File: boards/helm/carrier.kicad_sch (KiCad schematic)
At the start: 22 parts, among them J1 OPI_Z3_26PIN, J10 AUX 5V (screen), J16 BATT 12V, J2 OPI_BREAKOUT, J3 UART5 ttyAS5, J4 UART2 ttyAS2, J8 I2C3 spare, J9 FAN 5V, Q1 IRF9540N, U5 XL4015 5A

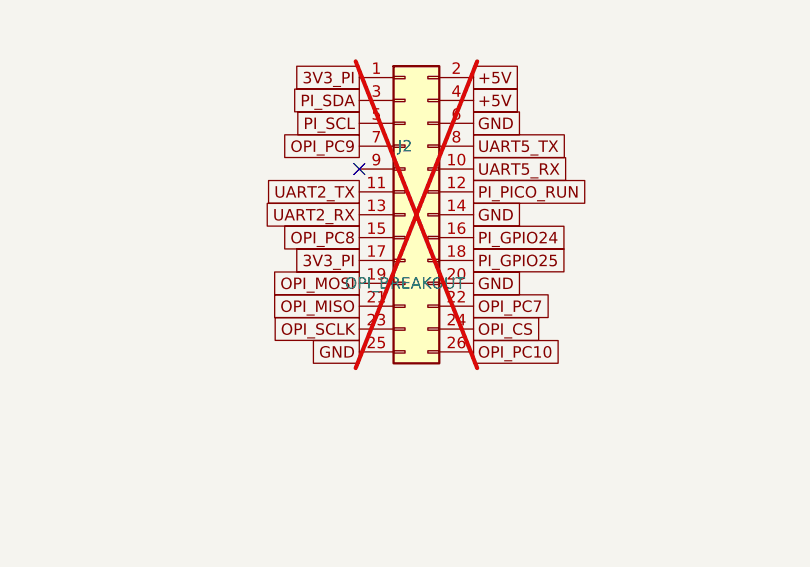
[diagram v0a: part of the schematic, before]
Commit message: feat(helm): J2 doubles as Raspberry Pi port (classic 26-pin positions), silk + docs
The PI26 net map already follows the classic RPi 26-pin layout, so a
Raspberry Pi (40-pin header pins 1-26) drops onto J2 via the same 26-way
IDC ribbon: power, Pico I2C link (SDA1/SCL1), console UART (TXD0/RXD0),
SPI and SWD/RUN GPIOs all line up. Fit one SBC only; J4 'UART2' JST is
bit-bang-only on an RPi (pins 11/13 are plain GPIOs there).

Co-Authored-By: Claude Fable 5 <noreply@anthropic.com>
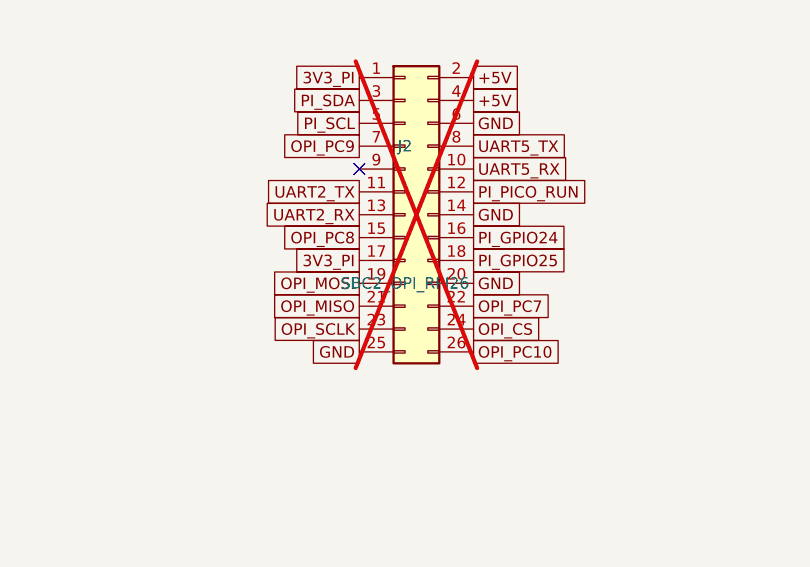
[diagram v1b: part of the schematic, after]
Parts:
- J2: value OPI_BREAKOUT -> SBC2_OPI_RPI26
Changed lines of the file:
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@@
     (property "Reference" "J2" (at 149.86 196.85 0)
       (effects (font (size 1.27 1.27))))
-    (property "Value" "OPI_BREAKOUT" (at 149.86 212.09 0)
+    (property "Value" "SBC2_OPI_RPI26" (at 149.86 212.09 0)
       (effects (font (size 1.27 1.27))))
     (property "Footprint" "Connector_PinHeader_2.54mm:PinHeader_2x13_P2.54mm_Vertical" (at 149.86 204.47 0)

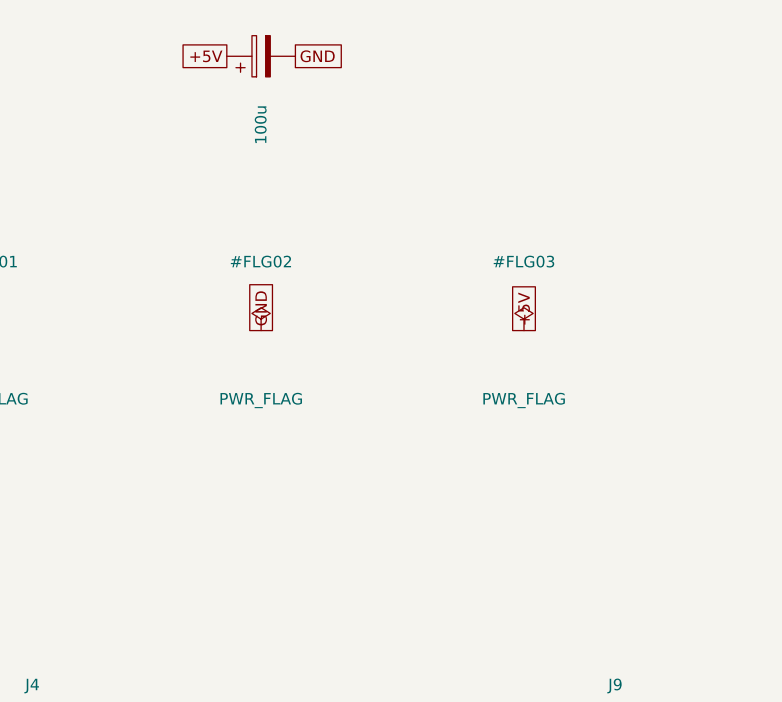
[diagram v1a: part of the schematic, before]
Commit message: feat(helm): NMEA2000/CAN provision — J5 power/shield connector, VIN tap, CAN-on-J12 docs
CAN rides the Pico 2 (can2040 on GP18/GP19); a 3.3V transceiver module
(Waveshare SN65HVD230) plugs J12 pins 1/8/6/7. New J5 XH-3 lands the N2K
drop cable's V+/GND/SHIELD; R41 (0R DNP) optionally powers the backbone
from VIN, R42 (0R DNP) bonds shield to GND. DRC 0/0.

Co-Authored-By: Claude Fable 5 <noreply@anthropic.com>
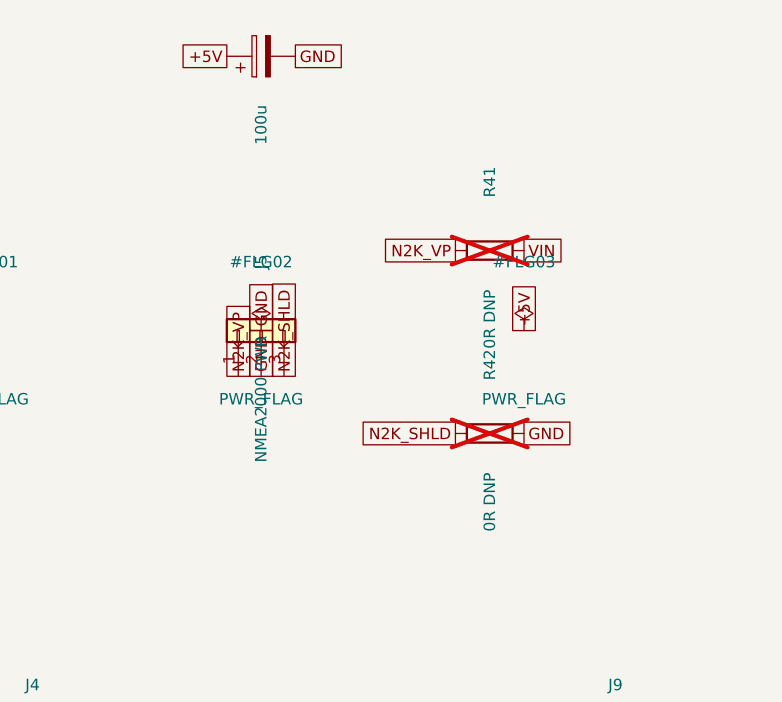
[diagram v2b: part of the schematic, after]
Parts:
- added J5: NMEA2000 PWR, Connector_JST:JST_XH_B3B-XH-A_1x03_P2.50mm_Vertical, symbol Connector_Generic:Conn_01x03
- added R41, R42: 0R DNP, Resistor_SMD:R_0805_2012Metric, symbol Device:R
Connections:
- net GND: now also J5.2 (Pin_2), R42.2
- net VIN: now also R41.2
- new net N2K_SHLD: J5.3 (Pin_3), R42.1
- new net N2K_VP: J5.1 (Pin_1), R41.1
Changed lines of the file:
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@@
     (effects (font (size 2 2) (bold yes)) (justify left bottom))
+  )
+  (symbol (lib_id "Connector_Generic:Conn_01x03") (at 330.2 138.43 90) (unit 1)
+    (exclude_from_sim no) (in_bom yes) (on_board yes) (dnp no)
+    (property "Reference" "J5" (at 330.2 130.81 0)
+      (effects (font (size 1.27 1.27))))
+    (property "Value" "NMEA2000 PWR" (at 330.2 146.05 0)
+      (effects (font (size 1.27 1.27))))
+    (property "Footprint" "Connector_JST:JST_XH_B3B-XH-A_1x03_P2.50mm_Vertical" (at 330.2 138.43 0)
+      (effects (font (size 1.27 1.27)) (hide yes)))
+    (property "Datasheet" "" (at 330.2 138.43 0)
+      (effects (font (size 1.27 1.27)) (hide yes)))
+    (property "MPN" "JST B4B-XH-A(LF)(SN)" (at 330.2 138.43 0)
+      (effects (font (size 1.27 1.27)) (hide yes)))
+    (pin "1")
+    (pin "2")
+    (pin "3")
+    (instances (project "vanchor-helm" (path "/a0000000-0000-4000-8000-000000000001/c0000000-0000-4000-8000-000000000002" (reference "J5") (unit 1))))
+  )
+  (symbol (lib_id "Device:R") (at 355.6 129.54 90) (unit 1)
+    (exclude_from_sim no) (in_bom yes) (on_board yes) (dnp yes)
+    (property "Reference" "R41" (at 355.6 121.92 0)
+      (effects (font (size 1.27 1.27))))
+    (property "Value" "0R DNP" (at 355.6 137.16 0)
+      (effects (font (size 1.27 1.27))))
+    (property "Footprint" "Resistor_SMD:R_0805_2012Metric" (at 355.6 129.54 0)
+      (effects (font (size 1.27 1.27)) (hide yes)))
+    (property "Datasheet" "" (at 355.6 129.54 0)
+      (effects (font (size 1.27 1.27)) (hide yes)))
+    (pin "1")
+    (pin "2")
+    (instances (project "vanchor-helm" (path "/a0000000-0000-4000-8000-000000000001/c0000000-0000-4000-8000-000000000002" (reference "R41") (unit 1))))
+  )
+  (symbol (lib_id "Device:R") (at 355.6 149.86 90) (unit 1)
+    (exclude_from_sim no) (in_bom yes) (on_board yes) (dnp yes)
+    (property "Reference" "R42" (at 355.6 142.24 0)
+      (effects (font (size 1.27 1.27))))
+    (property "Value" "0R DNP" (at 355.6 157.48 0)
+      (effects (font (size 1.27 1.27))))
+    (property "Footprint" "Resistor_SMD:R_0805_2012Metric" (at 355.6 149.86 0)
+      (effects (font (size 1.27 1.27)) (hide yes)))
+    (property "Datasheet" "" (at 355.6 149.86 0)
+      (effects (font (size 1.27 1.27)) (hide yes)))
+    (pin "1")
+    (pin "2")
+    (instances (project "vanchor-helm" (path "/a0000000-0000-4000-8000-000000000001/c0000000-0000-4000-8000-000000000002" (reference "R42") (unit 1))))
   )
   (symbol (lib_id "Connector_Generic:Conn_01x02") (at 44.45 69.85 0) (unit 1)
@@
     (instances (project "vanchor-helm" (path "/a0000000-0000-4000-8000-000000000001/c0000000-0000-4000-8000-000000000002" (reference "#FLG04") (unit 1))))
   )
+  (global_label "N2K_VP" (shape passive) (at 327.66 143.51 270.0) (fields_autoplaced yes)
+    (effects (font (size 1.27 1.27)) (justify left))
+    (property "Intersheetrefs" "${INTERSHEET_REFS}" (at 327.66 143.51 0)
+      (effects (font (size 1.27 1.27)) (hide yes)))
+  )
+  (global_label "GND" (shape passive) (at 330.2 143.51 270.0) (fields_autoplaced yes)
+    (effects (font (size 1.27 1.27)) (justify left))
+    (property "Intersheetrefs" "${INTERSHEET_REFS}" (at 330.2 143.51 0)
+      (effects (font (size 1.27 1.27)) (hide yes)))
+  )
+  (global_label "N2K_SHLD" (shape passive) (at 332.74 143.51 270.0) (fields_autoplaced yes)
+    (effects (font (size 1.27 1.27)) (justify left))
+    (property "Intersheetrefs" "${INTERSHEET_REFS}" (at 332.74 143.51 0)
+      (effects (font (size 1.27 1.27)) (hide yes)))
+  )
+  (global_label "N2K_VP" (shape passive) (at 351.79 129.54 180.0) (fields_autoplaced yes)
+    (effects (font (size 1.27 1.27)) (justify right))
+    (property "Intersheetrefs" "${INTERSHEET_REFS}" (at 351.79 129.54 0)
+      (effects (font (size 1.27 1.27)) (hide yes)))
+  )
+  (global_label "VIN" (shape passive) (at 359.41 129.54 0.0) (fields_autoplaced yes)
+    (effects (font (size 1.27 1.27)) (justify left))
+    (property "Intersheetrefs" "${INTERSHEET_REFS}" (at 359.41 129.54 0)
+      (effects (font (size 1.27 1.27)) (hide yes)))
+  )
+  (global_label "N2K_SHLD" (shape passive) (at 351.79 149.86 180.0) (fields_autoplaced yes)
+    (effects (font (size 1.27 1.27)) (justify right))
+    (property "Intersheetrefs" "${INTERSHEET_REFS}" (at 351.79 149.86 0)
+      (effects (font (size 1.27 1.27)) (hide yes)))
+  )
+  (global_label "GND" (shape passive) (at 359.41 149.86 0.0) (fields_autoplaced yes)
+    (effects (font (size 1.27 1.27)) (justify left))
+    (property "Intersheetrefs" "${INTERSHEET_REFS}" (at 359.41 149.86 0)
+      (effects (font (size 1.27 1.27)) (hide yes)))
+  )
   (label "BATT_IN" (at 39.37 69.85 180.0) (fields_autoplaced yes)

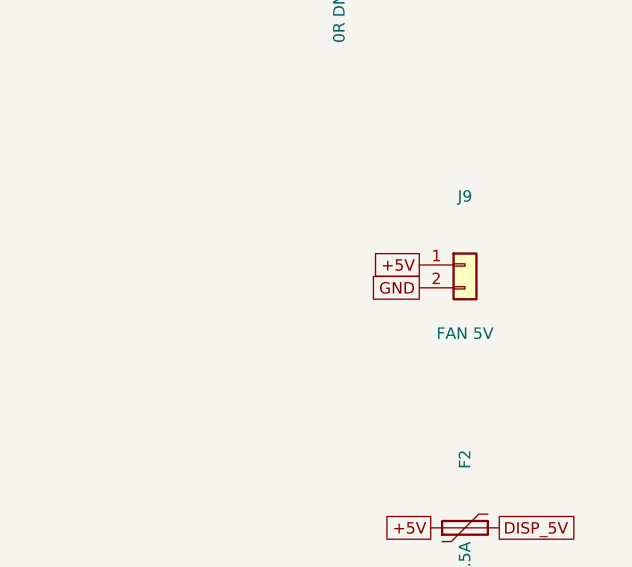
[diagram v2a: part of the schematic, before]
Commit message: feat(helm): steering-zero hall sensor input — J9 grows to 1x3 (5V/GND/SIG), 10k pullup + RC into Pico GP0
Open-collector hall switch (A3144 class) sees a magnet at servo center;
GP0 reads it (also broken out on J12.2; UART0 fallback = GP16/GP1).
Pour-redundant freerouted GND returns near J9/J10 removed. DRC 0/0.

Co-Authored-By: Claude Fable 5 <noreply@anthropic.com>
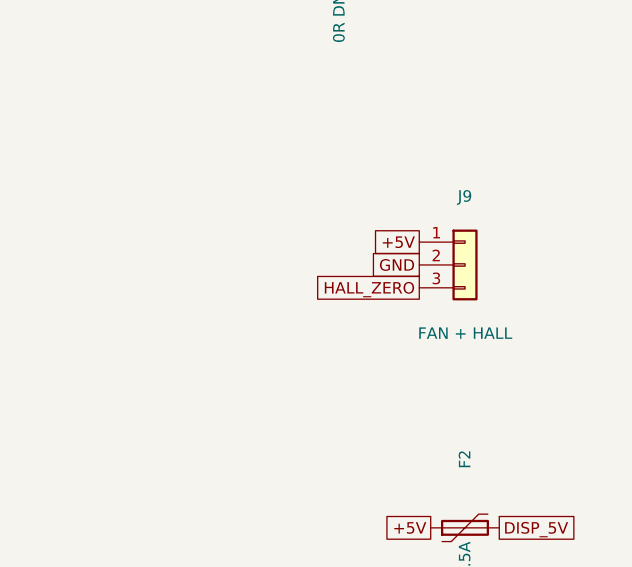
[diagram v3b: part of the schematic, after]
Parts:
- J9: value FAN 5V -> FAN + HALL; footprint Connector_PinHeader_2.54mm:PinHeader_1x02_P2.54mm_Vertical -> Connector_PinHeader_2.54mm:PinHeader_1x03_P2.54mm_Vertical; symbol Connector_Generic:Conn_01x02 -> Connector_Generic:Conn_01x03
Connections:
- new net HALL_ZERO: J9.3 (Pin_3)
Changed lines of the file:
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@@
     (instances (project "vanchor-helm" (path "/a0000000-0000-4000-8000-000000000001/c0000000-0000-4000-8000-000000000002" (reference "R6") (unit 1))))
   )
-  (symbol (lib_id "Connector_Generic:Conn_01x02") (at 369.57 185.42 0) (unit 1)
+  (symbol (lib_id "Connector_Generic:Conn_01x03") (at 369.57 185.42 0) (unit 1)
     (exclude_from_sim no) (in_bom yes) (on_board yes) (dnp no)
     (property "Reference" "J9" (at 369.57 177.8 0)
       (effects (font (size 1.27 1.27))))
-    (property "Value" "FAN 5V" (at 369.57 193.04 0)
-      (effects (font (size 1.27 1.27))))
-    (property "Footprint" "Connector_PinHeader_2.54mm:PinHeader_1x02_P2.54mm_Vertical" (at 369.57 185.42 0)
+    (property "Value" "FAN + HALL" (at 369.57 193.04 0)
+      (effects (font (size 1.27 1.27))))
+    (property "Footprint" "Connector_PinHeader_2.54mm:PinHeader_1x03_P2.54mm_Vertical" (at 369.57 185.42 0)
       (effects (font (size 1.27 1.27)) (hide yes)))
     (property "Datasheet" "" (at 369.57 185.42 0)
@@
     (pin "1")
     (pin "2")
+    (pin "3")
     (instances (project "vanchor-helm" (path "/a0000000-0000-4000-8000-000000000001/c0000000-0000-4000-8000-000000000002" (reference "J9") (unit 1))))
   )
@@
       (effects (font (size 1.27 1.27)) (hide yes)))
   )
-  (global_label "+5V" (shape passive) (at 364.49 185.42 180.0) (fields_autoplaced yes)
+  (global_label "+5V" (shape passive) (at 364.49 182.88 180.0) (fields_autoplaced yes)
+    (effects (font (size 1.27 1.27)) (justify right))
+    (property "Intersheetrefs" "${INTERSHEET_REFS}" (at 364.49 182.88 0)
+      (effects (font (size 1.27 1.27)) (hide yes)))
+  )
+  (global_label "GND" (shape passive) (at 364.49 185.42 180.0) (fields_autoplaced yes)
     (effects (font (size 1.27 1.27)) (justify right))
     (property "Intersheetrefs" "${INTERSHEET_REFS}" (at 364.49 185.42 0)
       (effects (font (size 1.27 1.27)) (hide yes)))
   )
-  (global_label "GND" (shape passive) (at 364.49 187.96 180.0) (fields_autoplaced yes)
+  (global_label "HALL_ZERO" (shape passive) (at 364.49 187.96 180.0) (fields_autoplaced yes)
     (effects (font (size 1.27 1.27)) (justify right))
     (property "Intersheetrefs" "${INTERSHEET_REFS}" (at 364.49 187.96 0)

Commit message: fix(helm): F2 polyfuse sits straight — custom MF-R250 footprint with in-line 5.1mm pads (KiCad's Bourns fps are stagger-lead), pour-redundant GND returns cleared. DRC 0/0
Co-Authored-By: Claude Fable 5 <noreply@anthropic.com>
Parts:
- F2: footprint Fuse:Fuse_Bourns_MF-RG300 -> vanchor-helm:MF-R250_Straight
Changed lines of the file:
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@@
     (property "Value" "MF-R250 2.5A" (at 369.57 222.25 0)
       (effects (font (size 1.27 1.27))))
-    (property "Footprint" "Fuse:Fuse_Bourns_MF-RG300" (at 369.57 214.63 0)
+    (property "Footprint" "vanchor-helm:MF-R250_Straight" (at 369.57 214.63 0)
       (effects (font (size 1.27 1.27)) (hide yes)))
     (property "Datasheet" "" (at 369.57 214.63 0)
